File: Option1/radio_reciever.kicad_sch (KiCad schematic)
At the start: 13 parts, among them J401 Conn_01x05_Pin, J402 Conn_01x04_Pin, J403 Conn_01x05_Pin, SW401 4*4*1.7

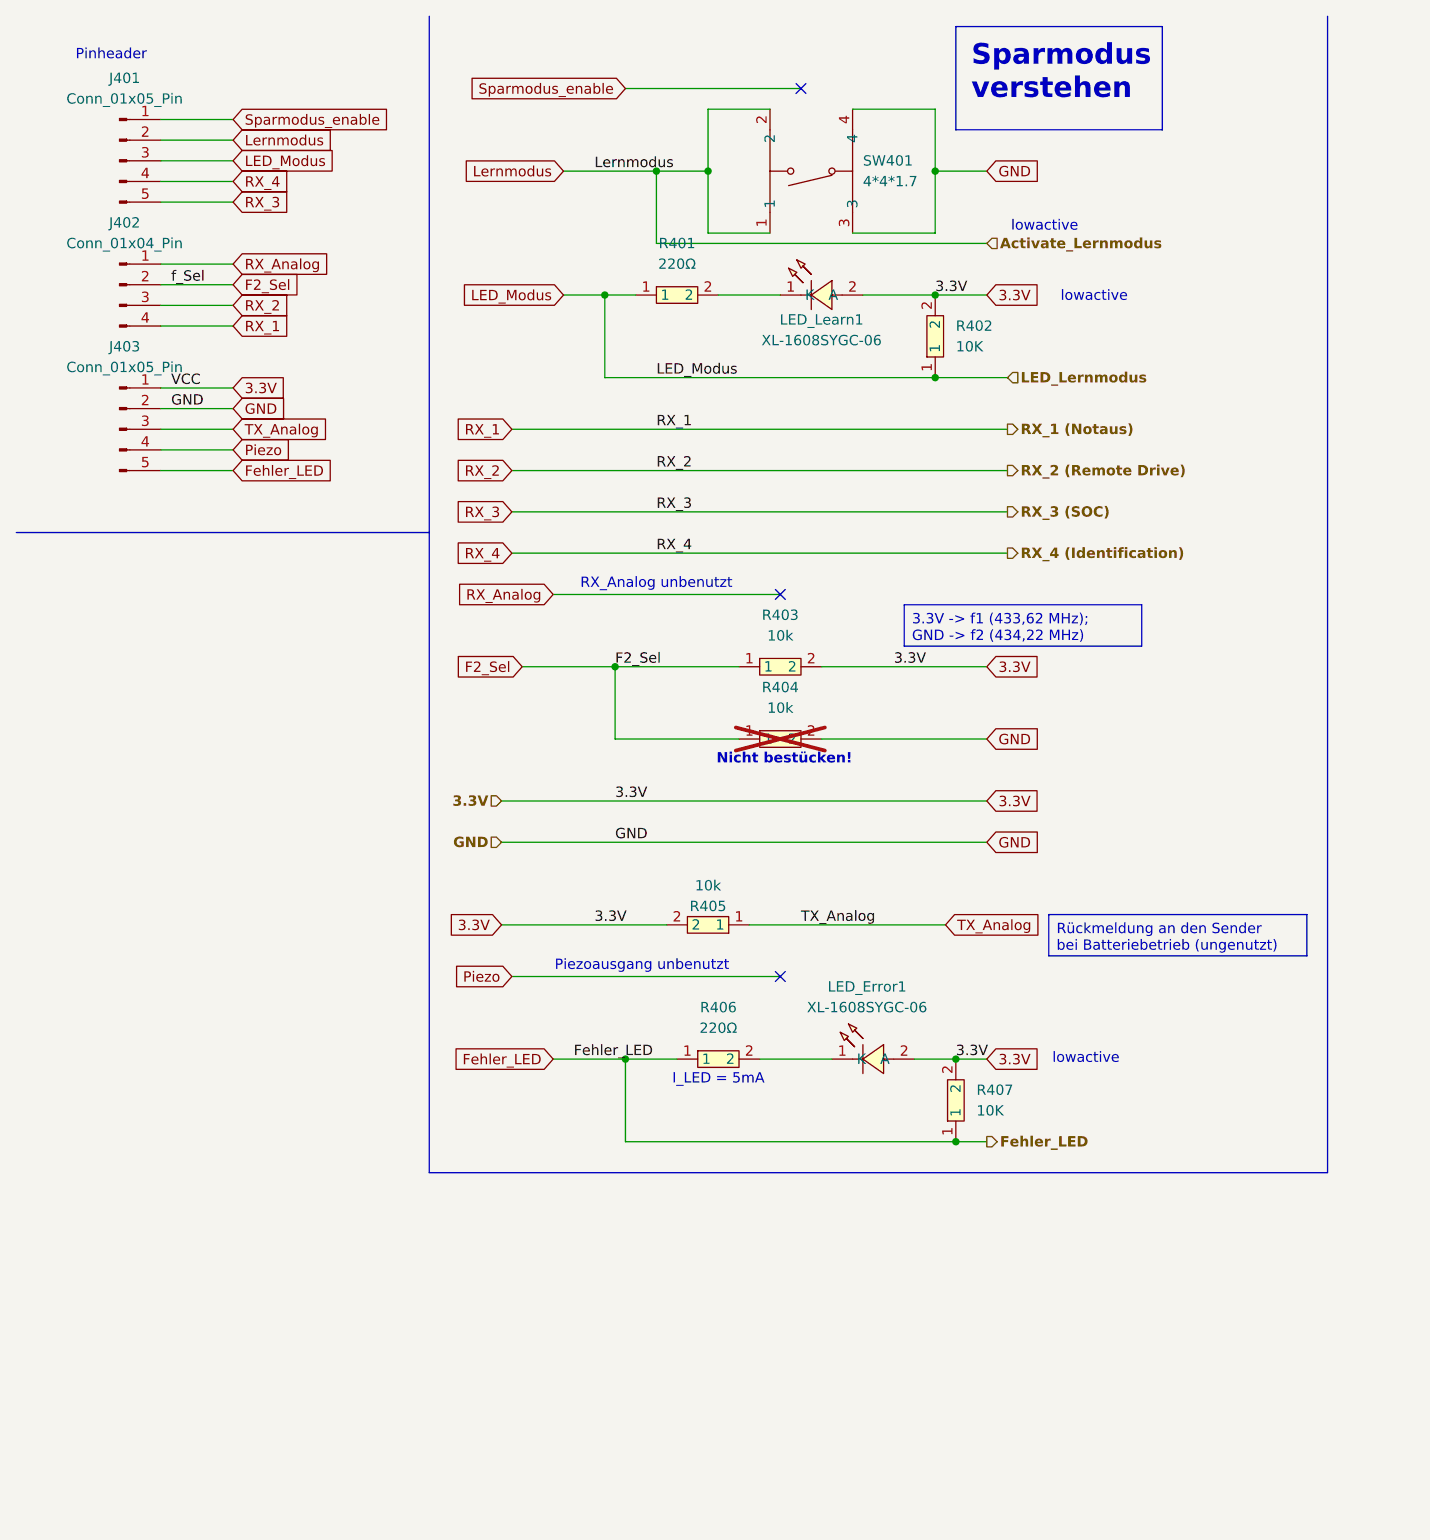
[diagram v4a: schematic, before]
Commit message: LEDs für RX Ausgänge des Funkmodules hinzugefügt
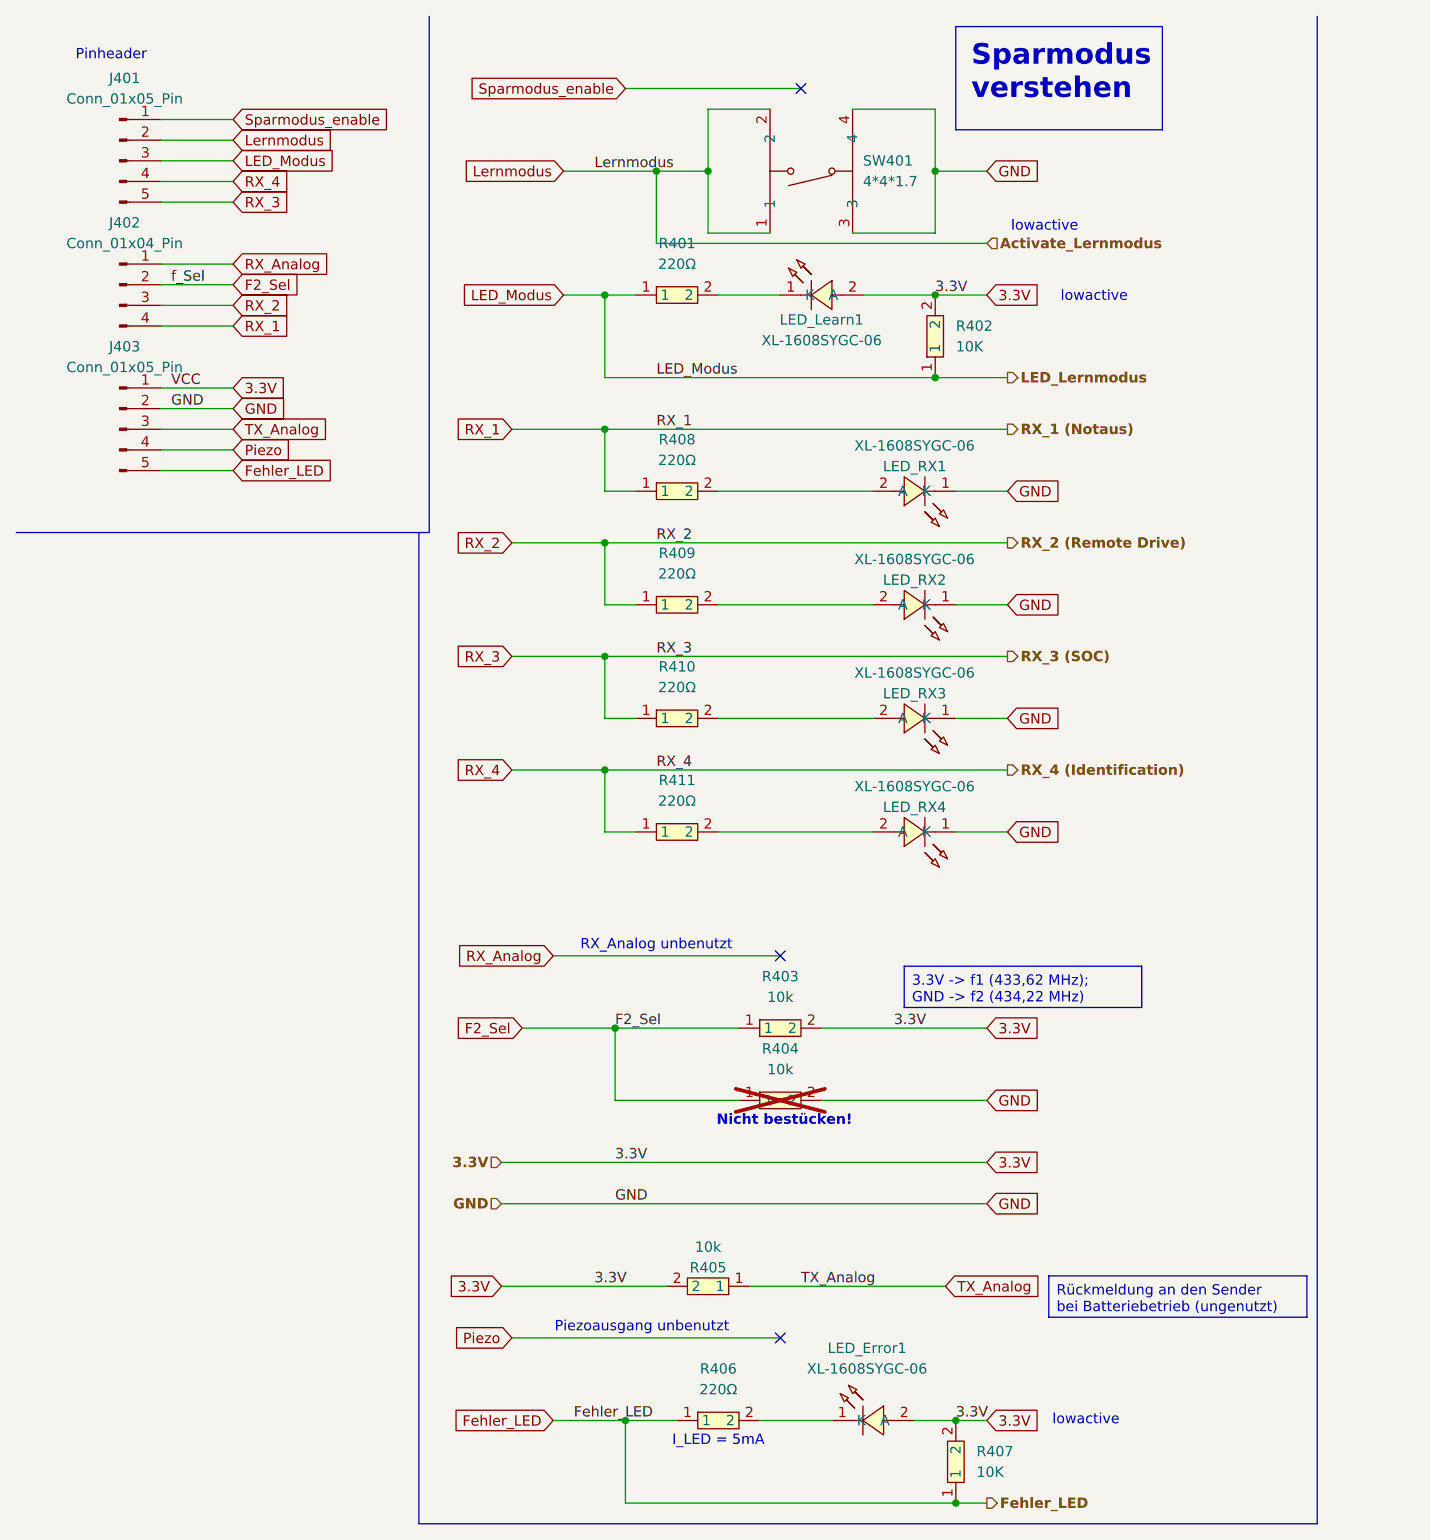
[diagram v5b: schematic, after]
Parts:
- added LED_RX1, LED_RX2, LED_RX3, LED_RX4: XL-1608SYGC-06, easyeda2kicad:LED0603-RD_GREEN, symbol EasyEda2KiCad:XL-1608SYGC-06
- added R408, R409, R410, R411: 220Ω, easyeda2kicad:R0603, symbol easyeda2kicad:0603WAF2200T5E
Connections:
- net GND: now also LED_RX1.1 (K), LED_RX2.1 (K), LED_RX3.1 (K), LED_RX4.1 (K)
- net RX_1: now also R408.1
- net RX_2: now also R409.1
- net RX_3: now also R410.1
- net RX_4: now also R411.1
- new net: LED_RX4.2 (A), R411.2
- new net: LED_RX1.2 (A), R408.2
- new net: LED_RX2.2 (A), R409.2
- new net: LED_RX3.2 (A), R410.2
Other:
- moved on the sheet: LED_Error1, R403, R404, R405, R406, R407

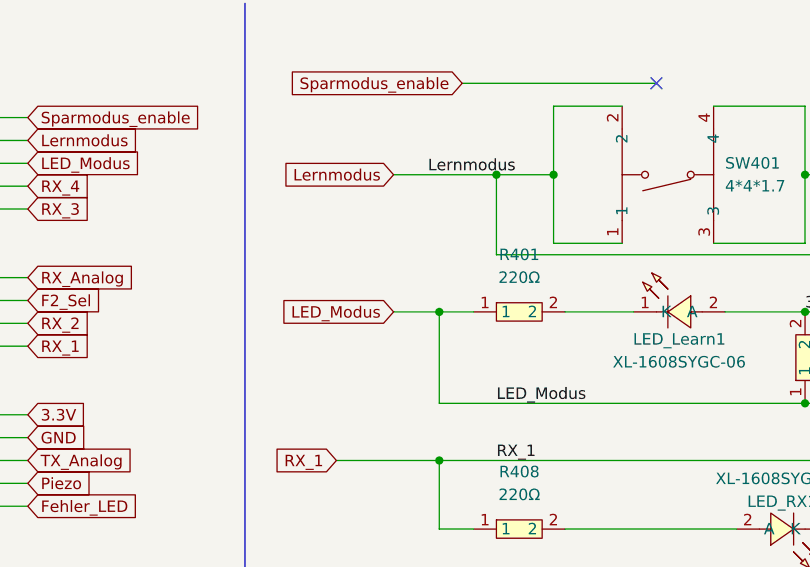
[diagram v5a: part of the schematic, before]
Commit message: Platine verkleinert, um besser in gehäuse zu passen, PullUp Widerstand an Button hinzugefügt
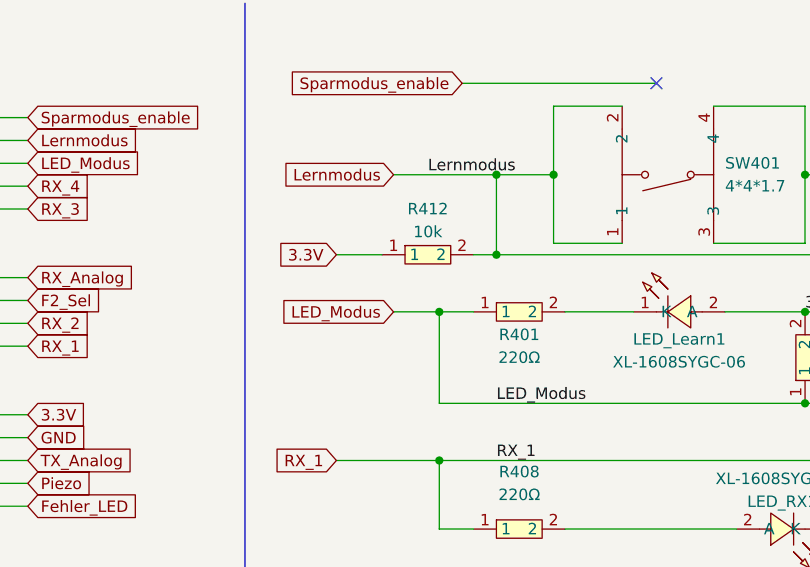
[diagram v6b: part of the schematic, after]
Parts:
- added R412: 10k, easyeda2kicad:R0603, symbol easyeda2kicad:0603WAF1002T5E
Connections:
- net 3.3V: now also R412.1
- net Lernmodus: now also R412.2
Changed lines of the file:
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@@
 	)
 	(junction
+		(at 91.44 40.64)
+		(diameter 0)
+		(color 0 0 0 0)
+	)
+	(junction
 		(at 85.09 91.44)
 		(diameter 0)
@@
 		)
 	)
+	(wire
+		(pts
+			(xy 73.66 40.64) (xy 78.74 40.64)
+		)
+		(stroke
+			(width 0)
+			(type default)
+		)
+	)
 	(polyline
 		(pts
@@
 	(wire
 		(pts
+			(xy 88.9 40.64) (xy 91.44 40.64)
+		)
+		(stroke
+			(width 0)
+			(type default)
+		)
+	)
+	(wire
+		(pts
 			(xy 73.66 77.47) (xy 85.09 77.47)
 		)
@@
 		)
 	)
+	(global_label "3.3V"
+		(shape input)
+		(at 73.66 40.64 180)
+		(fields_autoplaced yes)
+		(effects
+			(font
+				(size 1.27 1.27)
+			)
+			(justify right)
+		)
+		(property "Intersheetrefs" "${INTERSHEET_REFS}"
+			(at 66.5624 40.64 0)
+			(effects
+				(font
+					(size 1.27 1.27)
+				)
+				(justify right)
+				(hide yes)
+			)
+		)
+	)
 	(global_label "Sparmodus_enable"
 		(shape input)
@@
 		(on_board yes)
 		(dnp no)
-		(fields_autoplaced yes)
 		(property "Reference" "R401"
-			(at 93.98 40.64 0)
+			(at 93.98 49.53 0)
 			(effects
 				(font
@@
 		)
 		(property "Value" "220Ω"
-			(at 93.98 43.18 0)
+			(at 93.98 52.07 0)
 			(effects
 				(font
@@
 					(unit 1)
 				)
+			)
+		)
+	)
+	(symbol
+		(lib_id "easyeda2kicad:0603WAF1002T5E")
+		(at 83.82 40.64 0)
+		(unit 1)
+		(exclude_from_sim no)
+		(in_bom yes)
+		(on_board yes)
+		(dnp no)
+		(property "Reference" "R412"
+			(at 83.82 35.56 0)
+			(effects
+				(font
+					(size 1.27 1.27)
+				)
+			)
+		)
+		(property "Value" "10k"
+			(at 83.82 38.1 0)
+			(effects
+				(font
+					(size 1.27 1.27)
+				)
+			)
+		)
+		(property "Footprint" "easyeda2kicad:R0603"
+			(at 83.82 48.26 0)
+			(effects
+				(font
+					(size 1.27 1.27)
+				)
+				(hide yes)
+			)
+		)
+		(property "Datasheet" "https://lcsc.com/product-detail/Chip-Resistor-Surface-Mount-UniOhm_10KR-1002-1_C25804.html"
+			(at 83.82 50.8 0)
+			(effects
+				(font
+					(size 1.27 1.27)
+				)
+				(hide yes)
+			)
+		)
+		(property "Description" ""
+			(at 83.82 40.64 0)
+			(effects
+				(font
+					(size 1.27 1.27)
+				)
+				(hide yes)
+			)
+		)
+		(property "LCSC Part" "C25804"
+			(at 83.82 53.34 0)
+			(effects
+				(font
+					(size 1.27 1.27)
+				)
+				(hide yes)
+			)
+		)
+		(pin "1"
+		)
+		(pin "2"
+		)
+		(instances
+			(project ""
+				(path "/b9e5f262-9648-4b79-bdd1-af888b822329/23e58ba0-291f-4c3f-a823-9b20e599b3f1"
+					(reference "R412")
+					(unit 1)
+				)

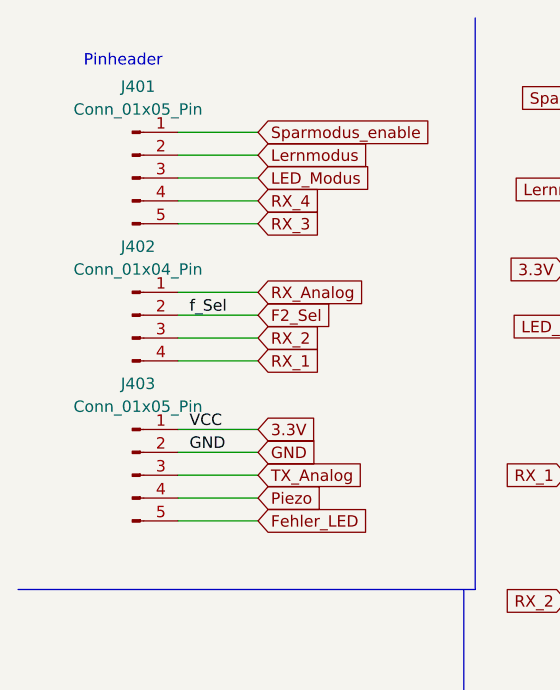
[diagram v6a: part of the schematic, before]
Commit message: Programming Header hinzugefügt für flashen via DevKit
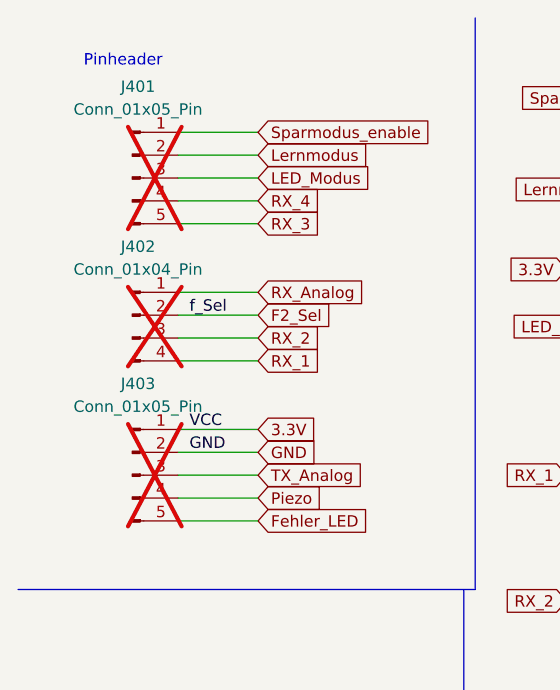
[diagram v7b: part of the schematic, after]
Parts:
- J401, J402, J403: now not fitted; now left out of the parts list
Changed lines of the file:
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@@
 		(unit 1)
 		(exclude_from_sim no)
-		(in_bom yes)
-		(on_board yes)
-		(dnp no)
+		(in_bom no)
+		(on_board yes)
+		(dnp yes)
 		(fields_autoplaced yes)
 		(property "Reference" "J402"
@@
 		(unit 1)
 		(exclude_from_sim no)
-		(in_bom yes)
-		(on_board yes)
-		(dnp no)
+		(in_bom no)
+		(on_board yes)
+		(dnp yes)
 		(fields_autoplaced yes)
 		(property "Reference" "J401"
@@
 		(unit 1)
 		(exclude_from_sim no)
-		(in_bom yes)
-		(on_board yes)
-		(dnp no)
+		(in_bom no)
+		(on_board yes)
+		(dnp yes)
 		(fields_autoplaced yes)
 		(property "Reference" "J403"

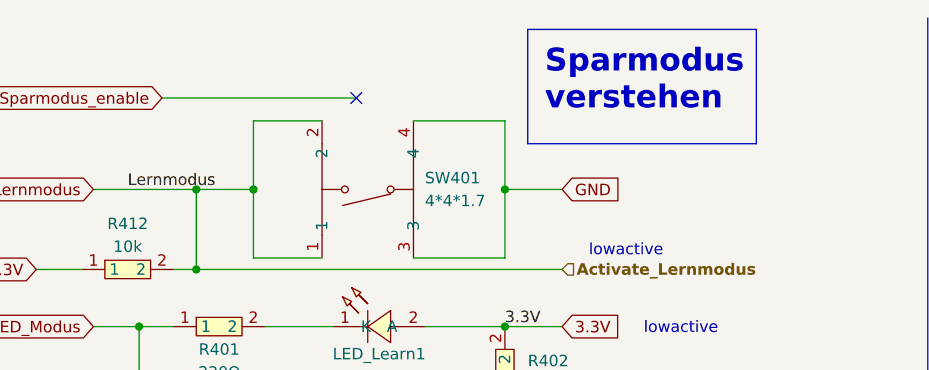
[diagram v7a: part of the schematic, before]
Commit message: Schaltplan zu bachelorarbeit Dokument hinzuigefügt. Fertigf bis SPI Flash
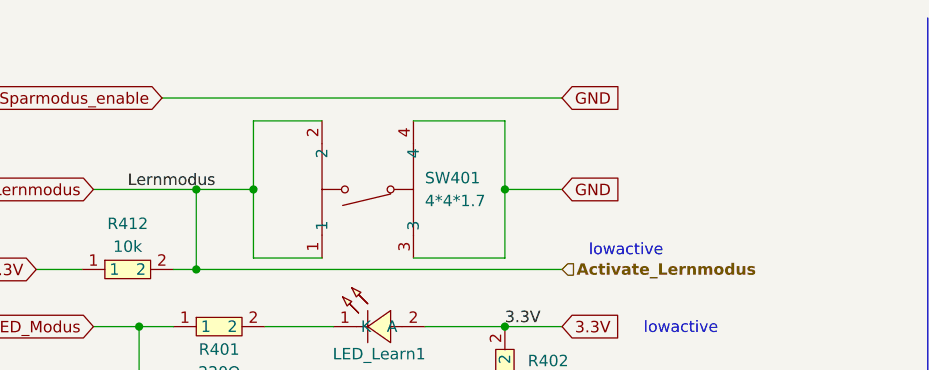
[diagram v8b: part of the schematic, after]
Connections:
- net Sparmodus_enable is gone; now on net GND: J401.1 (Pin_1)
- no-connect marks 3 -> 2
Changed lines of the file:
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@@
-		)
-	)
-	(text_box "Sparmodus verstehen"
-		(exclude_from_sim no)
-		(at 128.27 13.97 0)
-		(size 25.4 12.7)
-		(margins 1.905 1.905 1.905 1.905)
-		(stroke
-			(width 0)
-			(type default)
-		)
-		(fill
-			(type none)
-		)
-		(effects
-			(font
-				(size 2.54 2.54)
-				(thickness 0.508)
-				(bold yes)
-				(color 251 0 0 1)
-			)
-			(justify left top)
 		)
 	)
@@
 	)
 	(no_connect
-		(at 109.22 21.59)
-	)
-	(no_connect
 		(at 106.68 128.27)
 	)
@@
 	(wire
 		(pts
-			(xy 87.63 21.59) (xy 109.22 21.59)
+			(xy 87.63 21.59) (xy 132.08 21.59)
 		)
 		(stroke
@@
 				(hide yes)
 			)
+		)
+	)
+	(global_label "GND"
+		(shape input)
+		(at 132.08 21.59 0)
+		(fields_autoplaced yes)
+		(effects
+			(font
+				(size 1.27 1.27)
+			)
+			(justify left)
+		)
+		(property "Intersheetrefs" "${INTERSHEET_REFS}"
+			(at 138.9357 21.59 0)
+			(effects
+				(font
+					(size 1.27 1.27)
+				)
+				(justify left)
+				(hide yes)
+			)
